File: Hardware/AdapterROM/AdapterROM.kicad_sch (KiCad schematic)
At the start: 2 parts, among them J1 ROM, U1 28C256

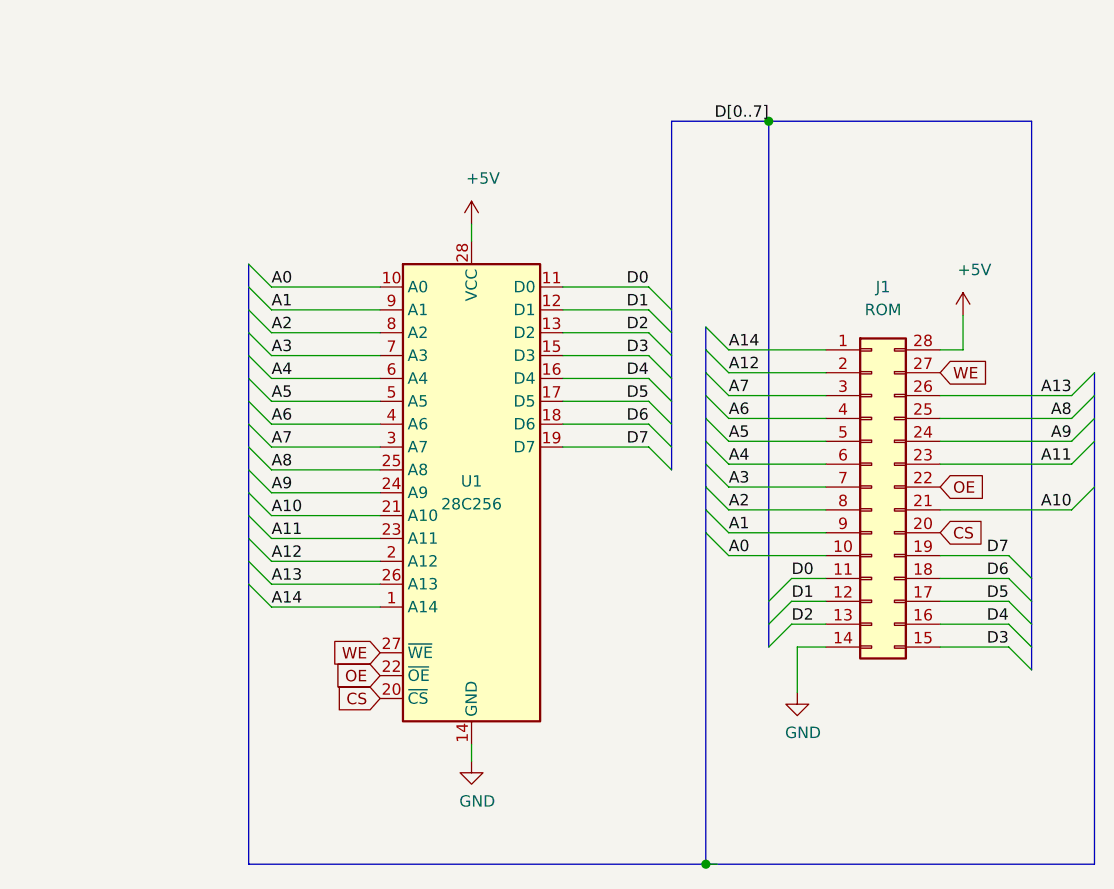
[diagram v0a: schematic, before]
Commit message: implement graphic loading from ROM
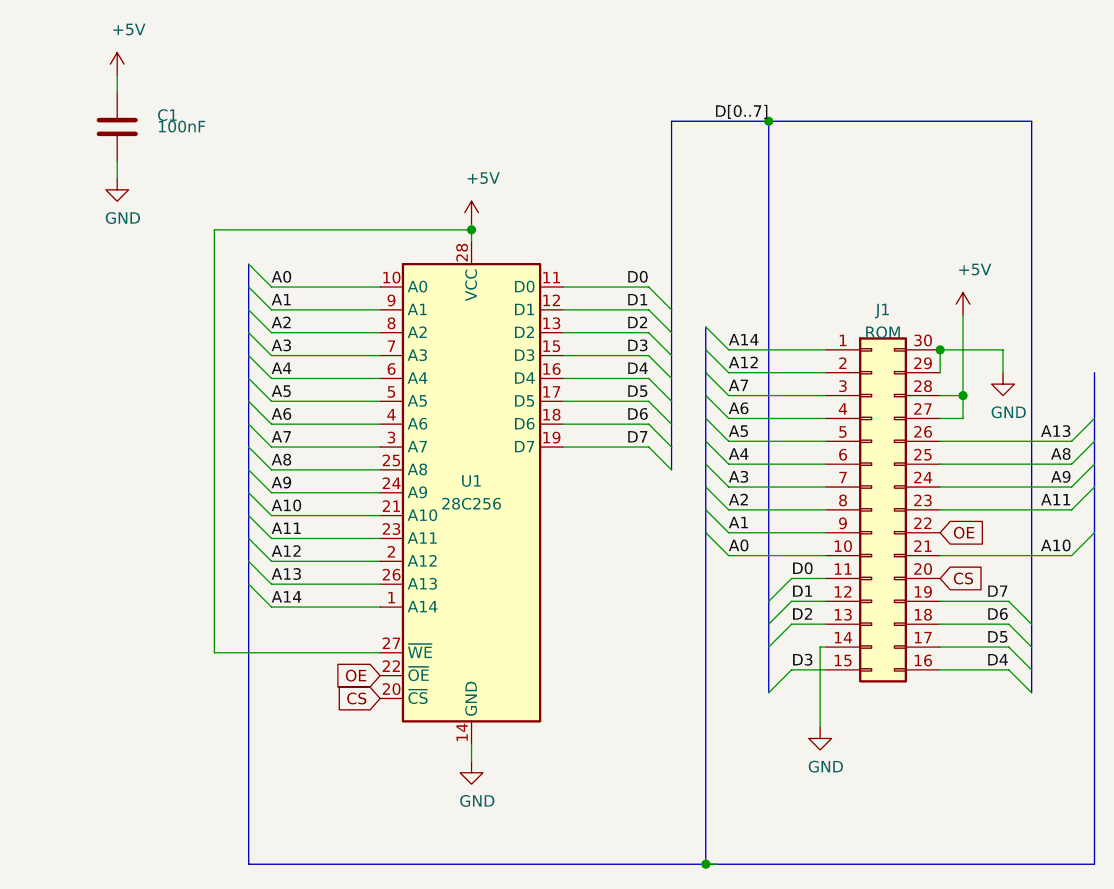
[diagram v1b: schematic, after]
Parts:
- added C1: 100nF, Capacitor_THT:C_Disc_D5.0mm_W2.5mm_P2.50mm, symbol Device:C
- J1: footprint Connector_PinHeader_2.54mm:PinHeader_2x14_P2.54mm_Horizontal -> Connector_PinHeader_2.54mm:PinHeader_2x15_P2.54mm_Horizontal; symbol Connector_Generic:Conn_02x14_Counter_Clockwise -> Connector_Generic:Conn_02x15_Counter_Clockwise
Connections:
- net WE is gone; now on net +5V: J1.27 (Pin_27), U1.27 (~WE)
- net +5V: now also C1.1
- net GND: now also J1.29 (Pin_29), J1.30 (Pin_30), C1.2

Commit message: New PLD logic, VGA, DMA ...
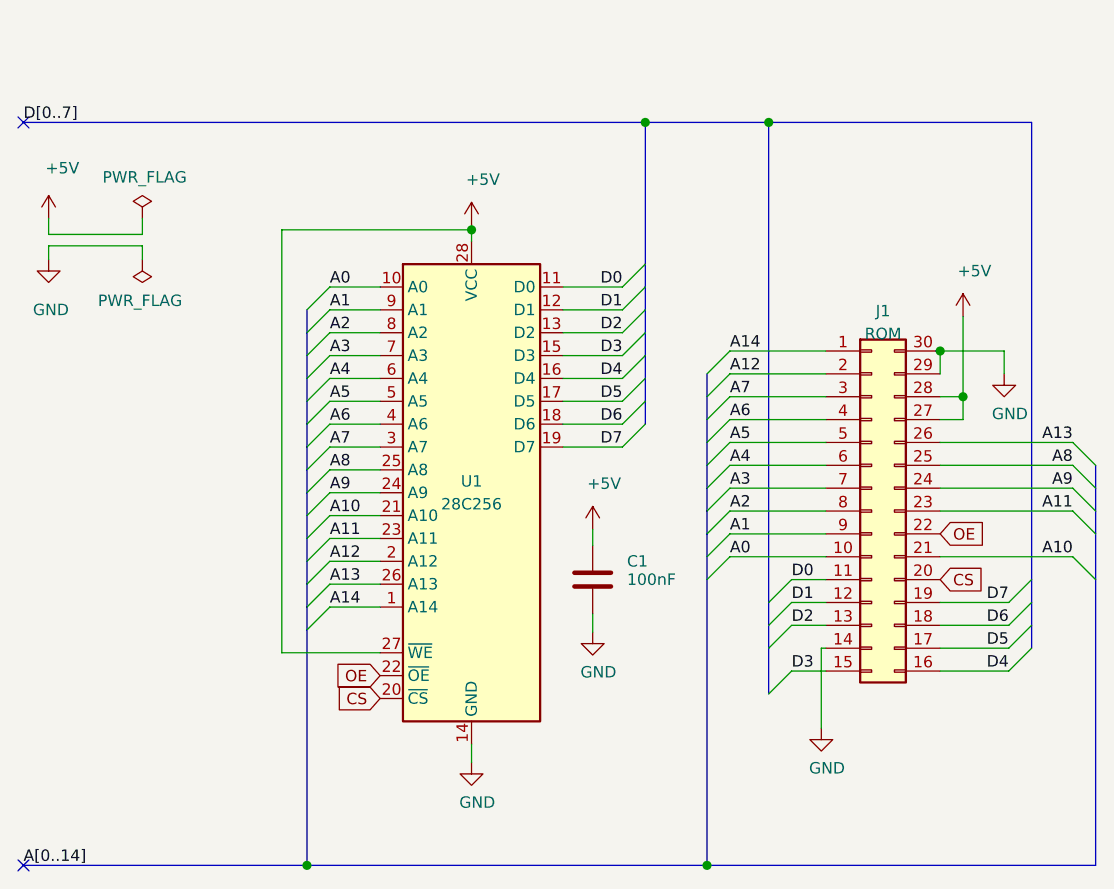
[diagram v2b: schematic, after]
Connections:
- no-connect marks 0 -> 2
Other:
- moved on the sheet: C1
